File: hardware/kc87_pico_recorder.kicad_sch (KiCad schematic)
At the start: 12 parts, among them J1 DIN-5_180degree, U1 LM358

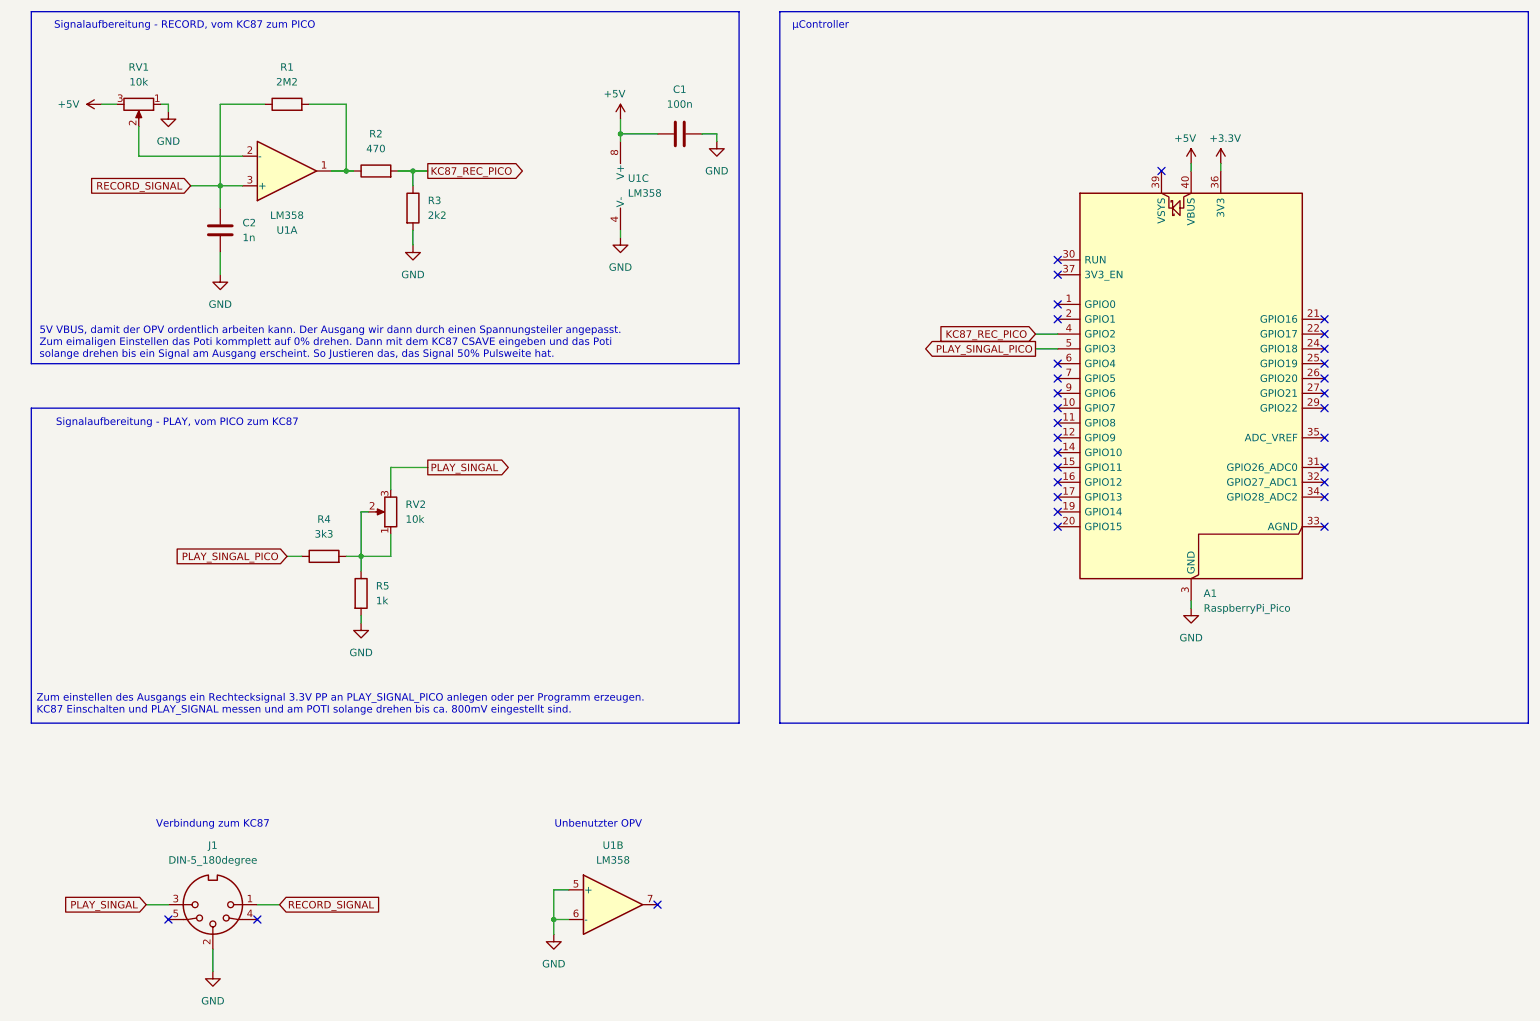
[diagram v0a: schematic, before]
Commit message: wip: new circuit for signal from kc87 to pico (a program save)
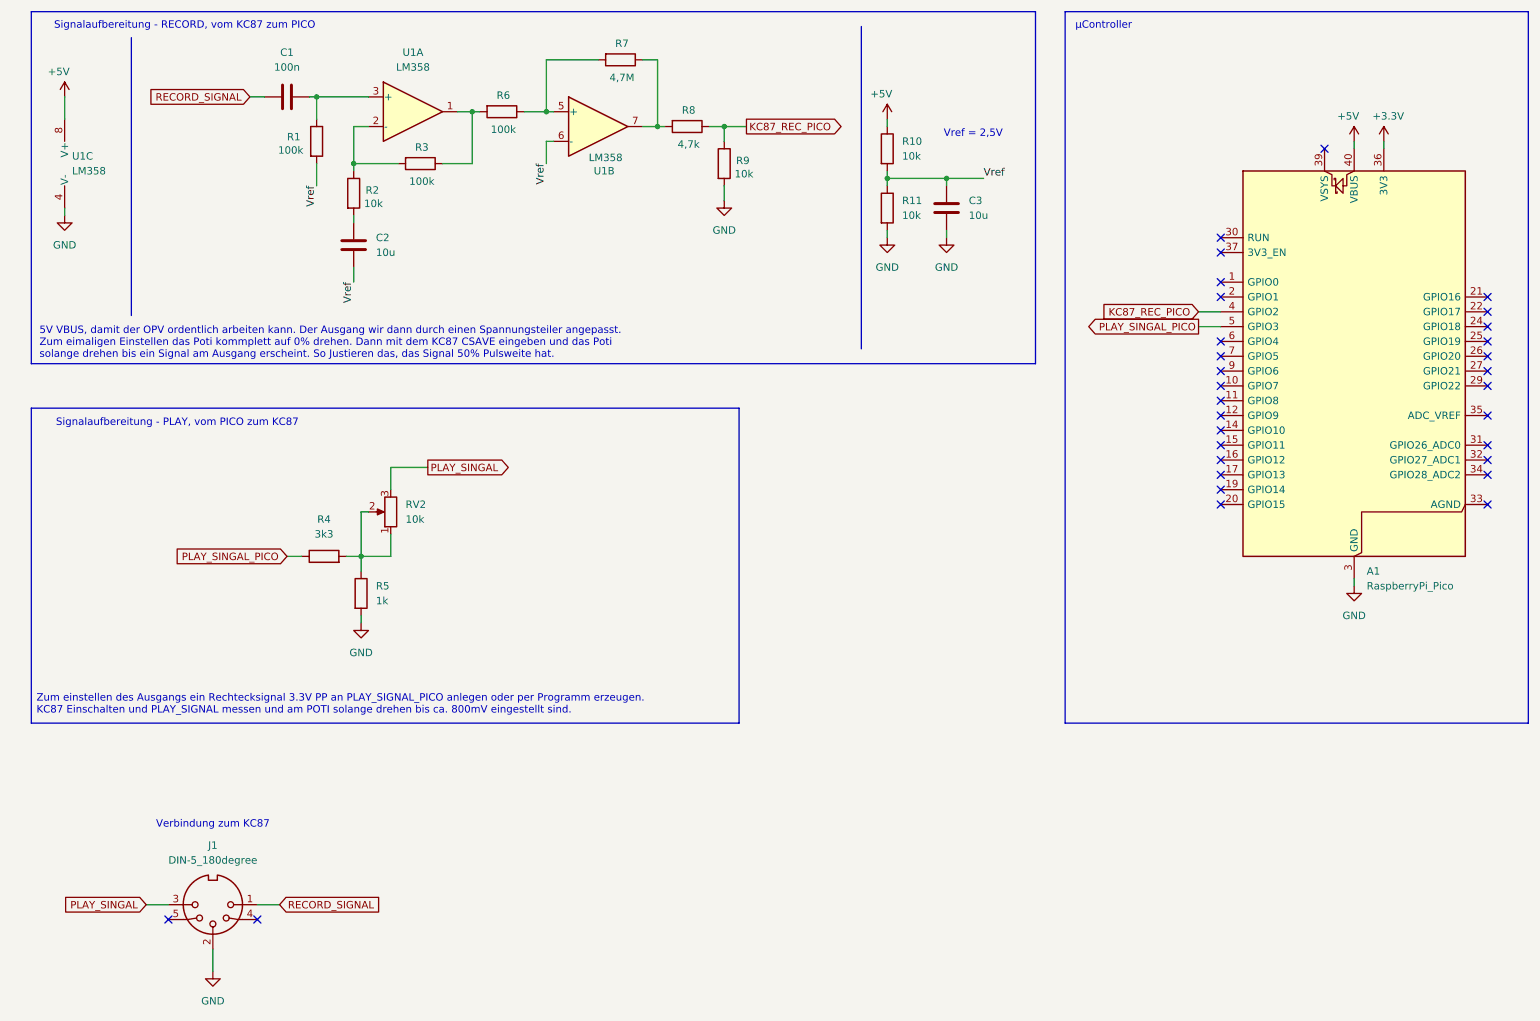
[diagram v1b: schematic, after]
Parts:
- removed RV1: 10k, symbol Device:R_Potentiometer
- added C3: 10u, symbol Device:C
- added R10, R11, R9: 10k, symbol Device:R
- added R6: 100k, symbol Device:R
- added R7: 4,7M, symbol Device:R
- added R8: 4,7k, symbol Device:R
- C1: footprint Capacitor_SMD:C_0805_2012Metric_Pad1.18x1.45mm_HandSolder -> (none)
- C2: value 1n -> 10u
- R1: value 2M2 -> 100k
- R2: value 470 -> 10k
- R3: value 2k2 -> 100k
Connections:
- net +5V: now also R10.1; no longer C1.1
- net GND: now also C3.1, R11.2, R9.2; no longer C1.2, C2.2, R3.2, U1.5 (+), U1.6 (-)
- net KC87_REC_PICO: now also R8.1, R9.1; no longer R2.2, R3.1
- net RECORD_SIGNAL: now also C1.1; no longer C2.1, R1.1, U1.3 (+)
- net at U1.7: now also R7.1, R8.2
- net at U1.2 (-): now also R2.1, R3.2
- new net: R3.1, R6.2, U1.1
- new net: C1.2, R1.1, U1.3 (+)
- new net: C2.2, R2.2
- new net: R6.1, R7.2, U1.5 (+)
- new net Vref: C2.1, C3.2, R1.2, R10.2, R11.1, U1.6 (-)
- no-connect marks 32 -> 31
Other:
- note added: "Vref = 2,5V"
- note removed: "Unbenutzter OPV"
- moved on the sheet: A1, U1B, U1C

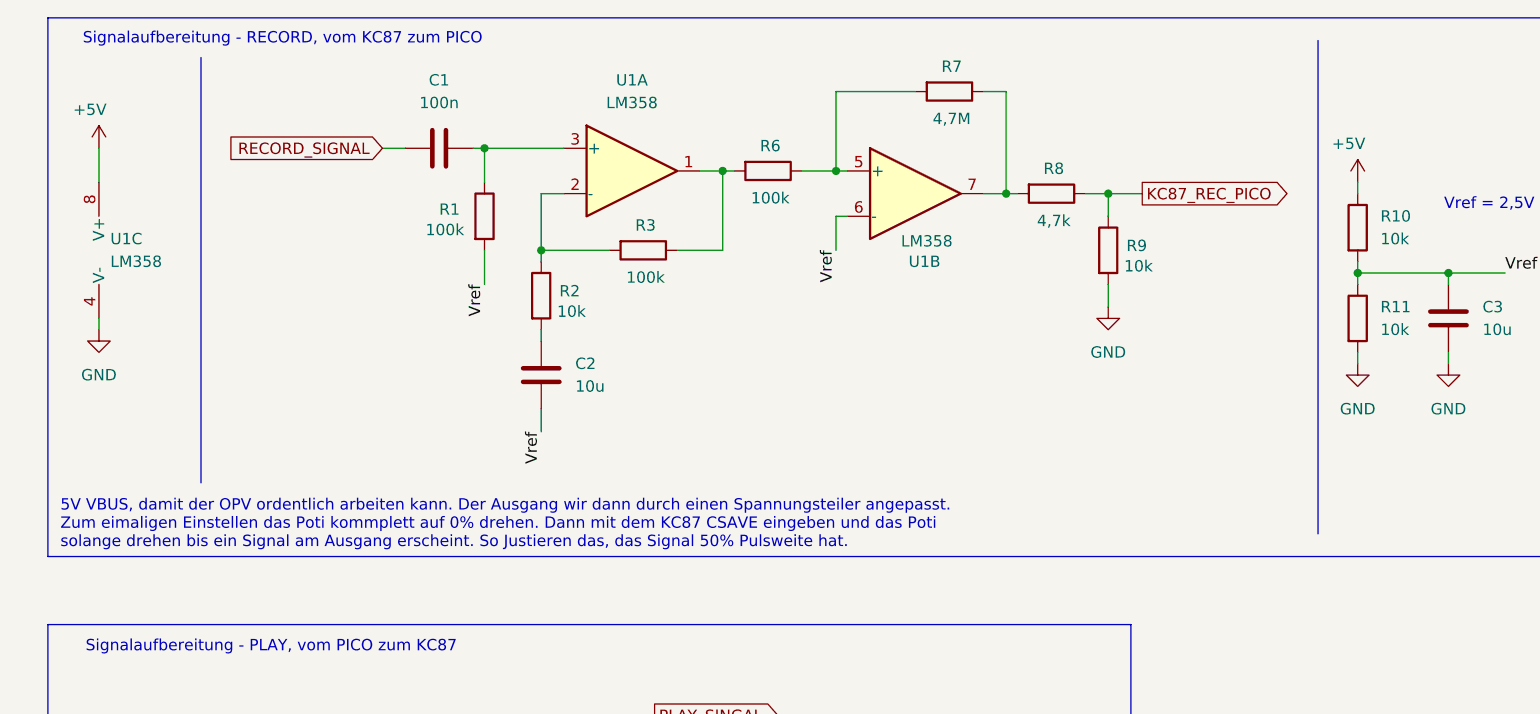
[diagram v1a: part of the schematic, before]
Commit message: add block decoder and TAP export to kc87tool
- kc87tool: new "decode" command (bytes, blocks, checksum, BASIC program
  name), TAP export for JKCEMU, remove SVG export
- README/doc: describe tape format, new record circuit and PC tool
- schematic: update note for the record circuit (no potentiometer anymore)
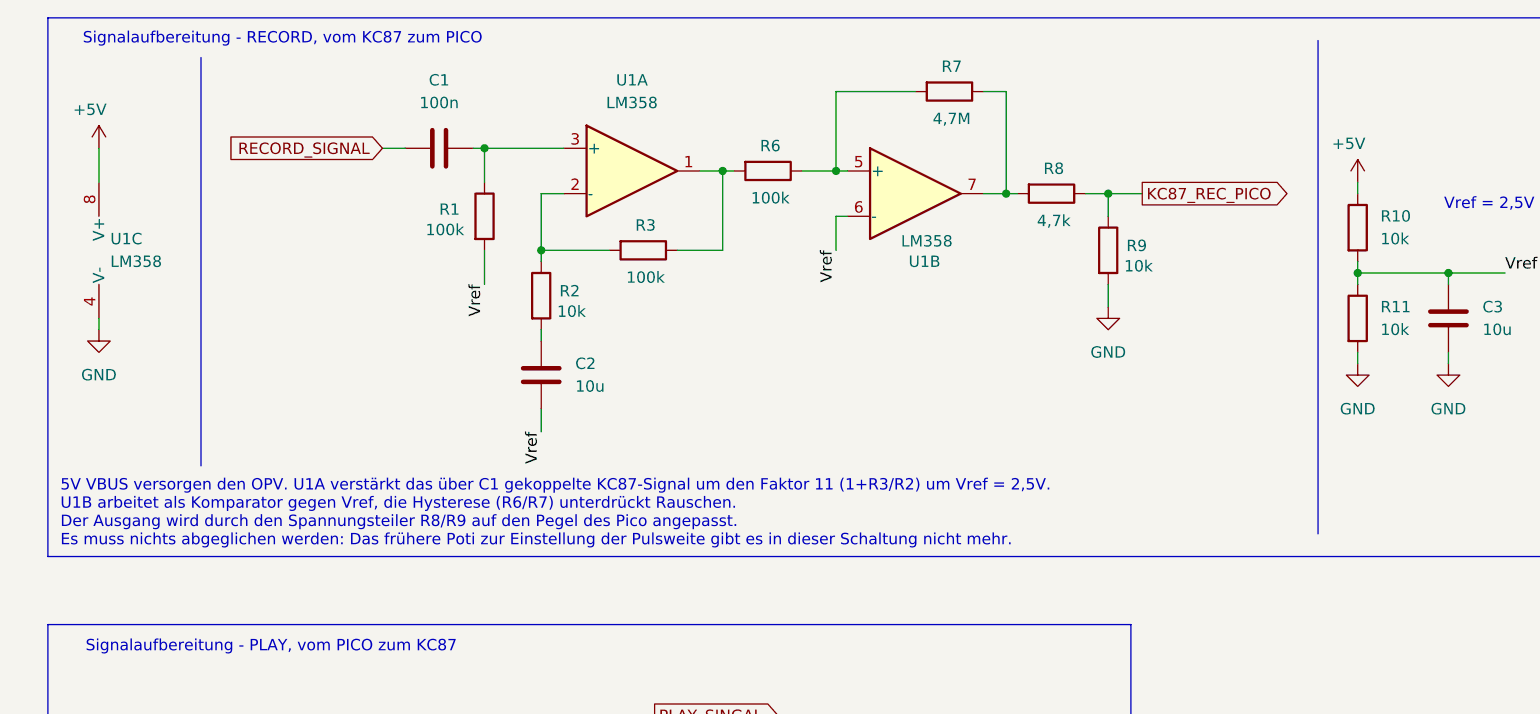
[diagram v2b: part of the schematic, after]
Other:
- note added: "5V VBUS versorgen den OPV. U1A verstärkt das über C1 gekoppelte KC87-Signal um den Faktor 11 (1+R3/R2) um Vref = 2,5V. U1B arbeitet als Komparator gegen Vref, die Hysterese (R6/R7) unterdrückt Rauschen. Der Ausgang wird durch den Spannungsteiler R8/R9 auf den Pegel des Pico angepasst. Es muss nichts abgeglichen werden: Das frühere Poti zur Einstellung der Pulsweite gibt es in dieser Schaltung nic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"
- note removed: "5V VBUS, damit der OPV ordentlich arbeiten kann. Der Ausgang wir dann durch einen Spannungsteiler angepasst. Zum eimaligen Einstellen das Poti kommplett auf 0% drehen. Dann mit dem KC87 CSAVE eingeben und das Poti solange drehen bis ein Signal am Ausgang erscheint. So Justieren das, das Signal 50% Pulsweite hat."
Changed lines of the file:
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@@
 		)
 	)
-	(text "5V VBUS, damit der OPV ordentlich arbeiten kann. Der Ausgang wir dann durch einen Spannungsteiler angepasst.\nZum eimaligen Einstellen das Poti kommplett auf 0% drehen. Dann mit dem KC87 CSAVE eingeben und das Poti\nsolange drehen bis ein Signal am Ausgang erscheint. So Justieren das, das Signal 50% Pulsweite hat."
-		(exclude_from_sim no)
-		(at 22.352 77.724 0)
+	(text "5V VBUS versorgen den OPV. U1A verstärkt das über C1 gekoppelte KC87-Signal um den Faktor 11 (1+R3/R2) um Vref = 2,5V.\nU1B arbeitet als Komparator gegen Vref, die Hysterese (R6/R7) unterdrückt Rauschen.\nDer Ausgang wird durch den Spannungsteiler R8/R9 auf den Pegel des Pico angepasst.\nEs muss nichts abgeglichen werden: Das frühere Poti zur Einstellung der Pulsweite gibt es in dieser Schaltung nicht mehr."
+		(exclude_from_sim no)
+		(at 22.352 76.5 0)
 		(effects
 			(font
@@
 	(polyline
 		(pts
-			(xy 38.1 25.4) (xy 38.1 73.025)
-		)
-		(stroke
+			(xy 38.1 25.4) (xy 38.1 71.12)
+		)
+		(stroke

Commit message: wip: added a play testprog and new circuit for signals to kc87
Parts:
- R4: value 3k3 -> 1k8
- R5: value 1k -> 180
- RV2: value 10k -> 1k
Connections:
- net at R4.2, RV2.1, RV2.2: no longer R5.1
- net PLAY_SINGAL renamed PLAY_SIGNAL
- net PLAY_SIGNAL: now also R5.1
- net PLAY_SINGAL_PICO renamed PLAY_SIGNAL_PICO
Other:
- note added: "Einstellen des Pegels: Rechtecksignal 3,3V PP an PLAY_SIGNAL_PICO anlegen (Test-Firmware kc87_play_test oder Playback-Programm). PLAY_SIGNAL mit dem Oszilloskop messen und mit RV2 auf ca. 250mV PP einstellen (Bereich ca. 200 bis 295mV PP) (KC87-Eingang: Re = 10k, Ue_ss min. 24mV; Recorder-Norm min. 200mV). R4 + RV2 bilden zusammen mit R5 einen Spannungsteiler, die Quellimpedanz am KC87 betraegt m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"
- note removed: "Zum einstellen des Ausgangs ein Rechtecksignal 3.3V PP an PLAY_SIGNAL_PICO anlegen oder per Programm erzeugen. KC87 Einschalten und PLAY_SIGNAL messen und am POTI solange drehen bis ca. 800mV eingestellt sind."
- moved on the sheet: R4, R5, RV2
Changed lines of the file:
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@@
 	(title_block
 		(title "KC87 Pico Recorder")
-		(date "2025-11-22")
+		(date "2026-10-25")
 		(rev "0.2")
 		(company "Thorsten Kattanek")
@@
 	(rectangle
 		(start 20.955 88.9)
-		(end 142.24 142.875)
+		(end 156.845 144.78)
 		(stroke
 			(width 0)
@@
 		)
 	)
-	(text "Zum einstellen des Ausgangs ein Rechtecksignal 3.3V PP an PLAY_SIGNAL_PICO anlegen oder per Programm erzeugen.\nKC87 Einschalten und PLAY_SIGNAL messen und am POTI solange drehen bis ca. 800mV eingestellt sind."
+	(text "Einstellen des Pegels: Rechtecksignal 3,3V PP an PLAY_SIGNAL_PICO anlegen (Test-Firmware kc87_play_test oder Playback-Programm).\nPLAY_SIGNAL mit dem Oszilloskop messen und mit RV2 auf ca. 250mV PP einstellen (Bereich ca. 200 bis 295mV PP)\n(KC87-Eingang: Re = 10k, Ue_ss min. 24mV; Recorder-Norm min. 200mV).\nR4 + RV2 bilden zusammen mit R5 einen Spannungsteiler, die Quellimpedanz am KC87 betraegt maximal ca. 180 Ohm."
 		(exclude_from_sim no)
 		(at 21.844 139.7 0)
@@
 	)
 	(junction
-		(at 77.47 114.3)
+		(at 76.2 119.38)
 		(diameter 0)
 		(color 0 0 0 0)
@@
 	)
 	(junction
+		(at 90.17 105.41)
+		(diameter 0)
+		(color 0 0 0 0)
+	)
+	(junction
 		(at 167.64 49.53)
 		(diameter 0)
@@
 	(wire
 		(pts
+			(xy 81.28 105.41) (xy 99.06 105.41)
+		)
+		(stroke
+			(width 0)
+			(type default)
+		)
+	)
+	(wire
+		(pts
 			(xy 69.85 39.37) (xy 69.85 35.56)
 		)
@@
 	(wire
 		(pts
-			(xy 64.77 114.3) (xy 67.31 114.3)
+			(xy 63.5 119.38) (xy 66.04 119.38)
 		)
 		(stroke
@@
 	(wire
 		(pts
-			(xy 88.9 99.06) (xy 82.55 99.06)
+			(xy 90.17 115.57) (xy 90.17 119.38)
 		)
 		(stroke
@@
 	(wire
 		(pts
-			(xy 77.47 124.46) (xy 77.47 125.73)
-		)
-		(stroke
-			(width 0)
-			(type default)
-		)
-	)
-	(wire
-		(pts
 			(xy 96.52 46.99) (xy 96.52 38.1)
 		)
@@
 	(wire
 		(pts
-			(xy 82.55 99.06) (xy 82.55 102.87)
+			(xy 81.28 105.41) (xy 81.28 107.95)
 		)
 		(stroke
@@
 	(wire
 		(pts
-			(xy 77.47 106.68) (xy 77.47 114.3)
+			(xy 76.2 111.76) (xy 76.2 119.38)
 		)
 		(stroke
@@
 	(wire
 		(pts
-			(xy 78.74 106.68) (xy 77.47 106.68)
+			(xy 77.47 111.76) (xy 76.2 111.76)
 		)
 		(stroke
@@
 	(wire
 		(pts
-			(xy 74.93 114.3) (xy 77.47 114.3)
+			(xy 73.66 119.38) (xy 76.2 119.38)
 		)
 		(stroke
@@
 	(wire
 		(pts
-			(xy 82.55 114.3) (xy 82.55 110.49)
+			(xy 81.28 119.38) (xy 81.28 115.57)
+		)
+		(stroke
+			(width 0)
+			(type default)
+		)
+	)
+	(wire
+		(pts
+			(xy 90.17 105.41) (xy 90.17 107.95)
 		)
 		(stroke
@@
 	(wire
 		(pts
-			(xy 77.47 114.3) (xy 82.55 114.3)
-		)
-		(stroke
-			(width 0)
-			(type default)
-		)
-	)
-	(wire
-		(pts
-			(xy 77.47 114.3) (xy 77.47 116.84)
+			(xy 76.2 119.38) (xy 81.28 119.38)
 		)
 		(stroke
@@
 		)
 	)
-	(global_label "PLAY_SINGAL_PICO"
+	(global_label "PLAY_SIGNAL_PICO"
 		(shape input)
-		(at 64.77 114.3 180)
+		(at 63.5 119.38 180)
 		(fields_autoplaced yes)
 		(effects
@@
 		)
 		(property "Intersheetrefs" "${INTERSHEET_REFS}"
-			(at 44.3675 114.3 0)
+			(at 43.0975 119.38 0)
 			(hide yes)
 			(show_name no)
@@
 		)
 	)
-	(global_label "PLAY_SINGAL"
+	(global_label "PLAY_SIGNAL"
 		(shape output)
-		(at 88.9 99.06 0)
+		(at 99.06 105.41 0)
 		(fields_autoplaced yes)
 		(effects
@@
 		)
 		(property "Intersheetrefs" "${INTERSHEET_REFS}"
-			(at 103.8596 99.06 0)
+			(at 114.0196 105.41 0)
 			(hide yes)
 			(show_name no)
@@
 		)
 	)
-	(global_label "PLAY_SINGAL"
+	(global_label "PLAY_SIGNAL"
 		(shape input)
 		(at 40.64 173.99 180)
@@
 		)
 	)
-	(global_label "PLAY_SINGAL_PICO"
+	(global_label "PLAY_SIGNAL_PICO"
 		(shape output)
 		(at 220.98 74.93 180)
@@
 	(symbol
 		(lib_id "Device:R")
-		(at 71.12 114.3 90)
+		(at 69.85 119.38 90)
 		(unit 1)
 		(body_style 1)
@@
 		(fields_autoplaced yes)
 		(property "Reference" "R4"
-			(at 71.12 107.95 90)
+			(at 69.85 113.03 90)
 			(show_name no)
 			(do_not_autoplace no)
@@
 			)
 		)
-		(property "Value" "3k3"
-			(at 71.12 110.49 90)
+		(property "Value" "1k8"
+			(at 69.85 115.57 90)
 			(show_name no)
 			(do_not_autoplace no)
@@
 		)
 		(property "Footprint" ""
-			(at 71.12 116.078 90)
+			(at 69.85 121.158 90)
 			(hide yes)
 			(show_name no)
@@
 		)
 		(property "Datasheet" ""
-			(at 71.12 114.3 0)
+			(at 69.85 119.38 0)
 			(hide yes)
 			(show_name no)
@@
 		)
 		(property "Description" "Resistor"
-			(at 71.12 114.3 0)
+			(at 69.85 119.38 0)
 			(hide yes)
 			(show_name no)
@@
 	(symbol
 		(lib_id "power:GND")
-		(at 77.47 125.73 0)
+		(at 90.17 119.38 0)
 		(unit 1)
 		(body_style 1)
@@
 		(fields_autoplaced yes)
 		(property "Reference" "#PWR011"
-			(at 77.47 132.08 0)
+			(at 90.17 125.73 0)
 			(hide yes)
 			(show_name no)
@@
 		)
 		(property "Value" "GND"
-			(at 77.47 130.81 0)
+			(at 90.17 124.46 0)
 			(show_name no)
 			(do_not_autoplace no)
@@
 		)
 		(property "Footprint" ""
-			(at 77.47 125.73 0)
+			(at 90.17 119.38 0)
 			(hide yes)
 			(show_name no)
@@
 		)
 		(property "Datasheet" ""
-			(at 77.47 125.73 0)
+			(at 90.17 119.38 0)
 			(hide yes)
 			(show_name no)
@@
 		)
 		(property "Description" "Power symbol creates a global label with name \"GND\" , ground"
-			(at 77.47 125.73 0)
+			(at 90.17 119.38 0)
 			(hide yes)
 			(show_name no)
@@
 	(symbol
 		(lib_id "Device:R_Potentiometer")
-		(at 82.55 106.68 180)
+		(at 81.28 111.76 180)
 		(unit 1)
 		(body_style 1)
@@
 		(fields_autoplaced yes)
 		(property "Reference" "RV2"
-			(at 85.09 105.4099 0)
+			(at 83.82 110.4899 0)
 			(show_name no)
 			(do_not_autoplace no)
@@
 			)
 		)
-		(property "Value" "10k"
-			(at 85.09 107.9499 0)
+		(property "Value" "1k"
+			(at 83.82 113.0299 0)
 			(show_name no)
 			(do_not_autoplace no)
@@
 		)
 		(property "Footprint" ""
-			(at 82.55 106.68 0)
+			(at 81.28 111.76 0)
 			(hide yes)
 			(show_name no)
@@
 		)
 		(property "Datasheet" ""
-			(at 82.55 106.68 0)
+			(at 81.28 111.76 0)
 			(hide yes)
 			(show_name no)
@@
 		)
 		(property "Description" "Potentiometer"
-			(at 82.55 106.68 0)
+			(at 81.28 111.76 0)
 			(hide yes)
 			(show_name no)
@@
 	(symbol
 		(lib_id "Device:R")
-		(at 77.47 120.65 0)
+		(at 90.17 111.76 0)
 		(unit 1)
 		(body_style 1)
@@
 		(fields_autoplaced yes)
 		(property "Reference" "R5"
-			(at 80.01 119.3799 0)
+			(at 92.71 110.4899 0)
 			(show_name no)
 			(do_not_autoplace no)
@@
 			)
 		)
-		(property "Value" "1k"
-			(at 80.01 121.9199 0)
+		(property "Value" "180"
+			(at 92.71 113.0299 0)
 			(show_name no)
 			(do_not_autoplace no)
@@
 		)
 		(property "Footprint" ""
-			(at 75.692 120.65 90)
+			(at 88.392 111.76 90)
 			(hide yes)
 			(show_name no)
@@
 		)
 		(property "Datasheet" ""
-			(at 77.47 120.65 0)
+			(at 90.17 111.76 0)
 			(hide yes)
 			(show_name no)
@@
 		)
 		(property "Description" "Resistor"
-			(at 77.47 120.65 0)
+			(at 90.17 111.76 0)
 			(hide yes)
 			(show_name no)
